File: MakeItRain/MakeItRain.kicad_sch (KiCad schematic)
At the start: 11 parts, among them J1 Conn_02x15_Odd_Even, J2 Conn_02x19_Odd_Even, J3 Conn_01x19

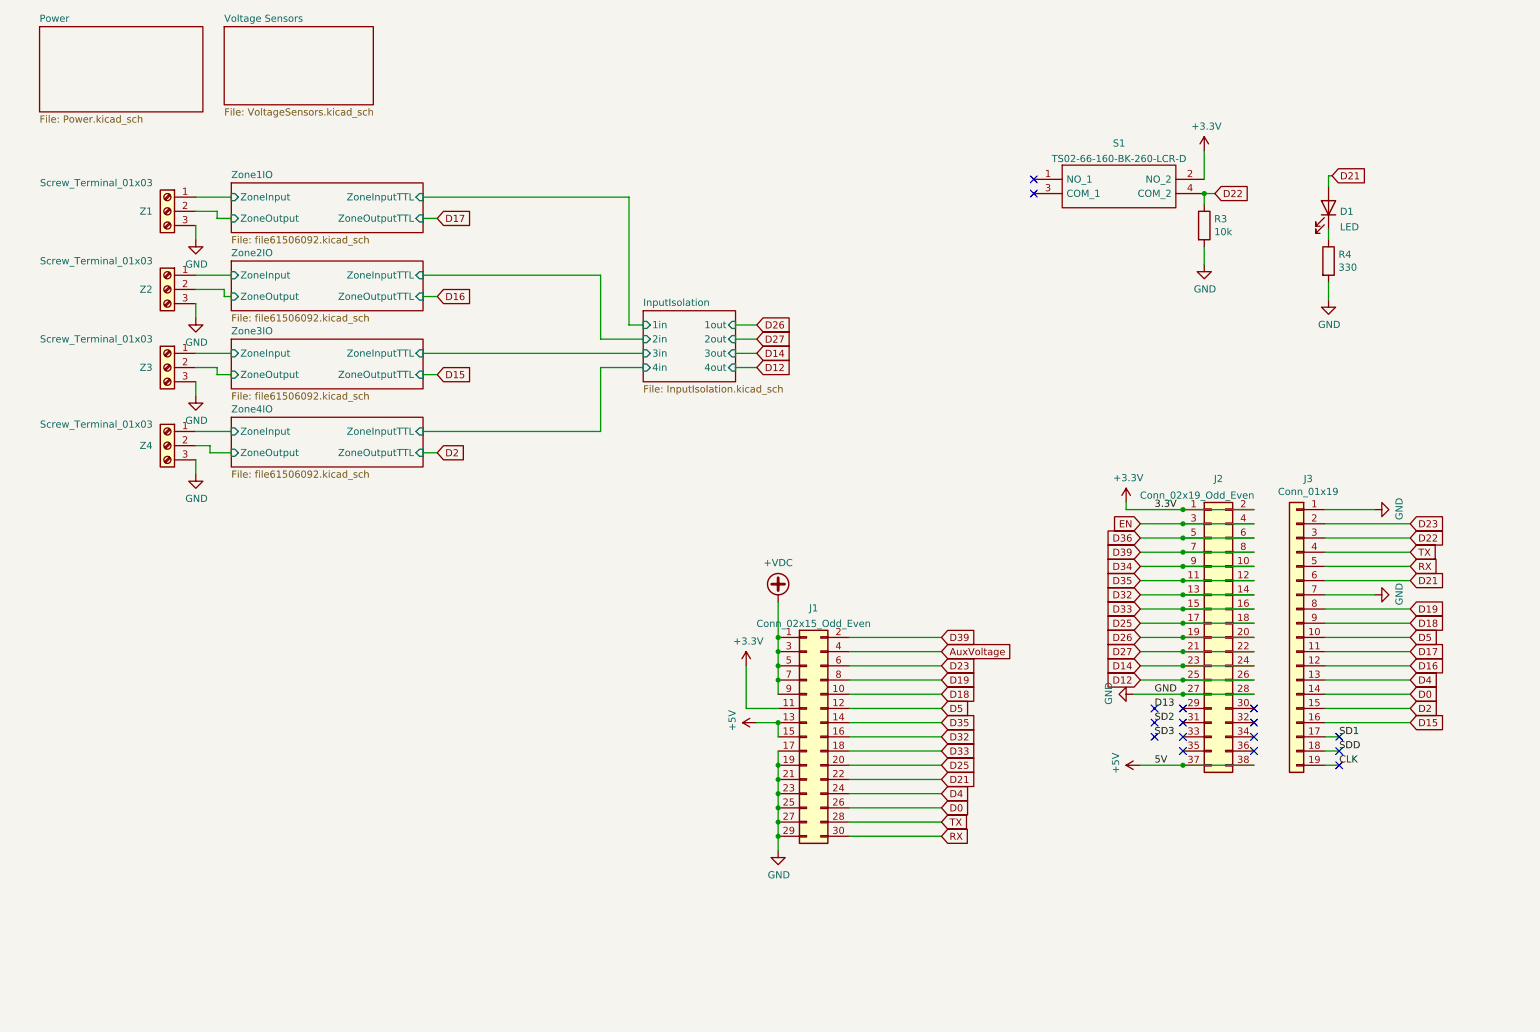
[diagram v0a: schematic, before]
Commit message: working on pin reassignment to fix the stupid stupid ways that esp32 are designed in hardware that require much in way of digging through docs cause not all gpio are created equal.
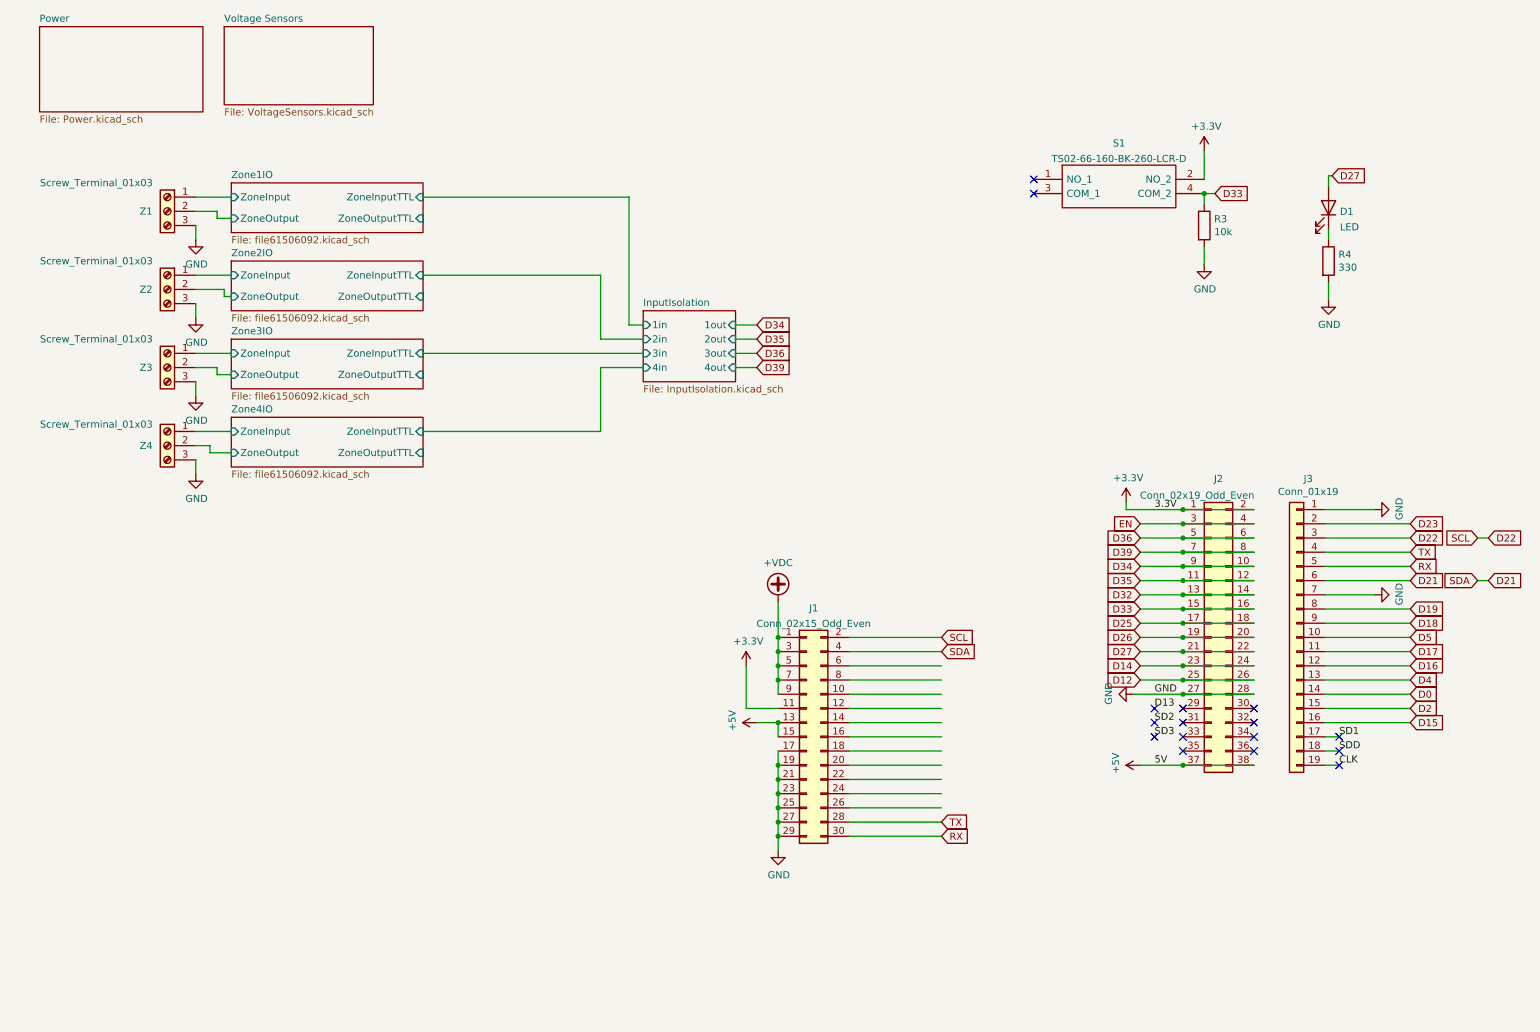
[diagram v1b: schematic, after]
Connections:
- net AuxVoltage is gone; now on net D21: J1.4 (Pin_4)
- net D0: no longer J1.26 (Pin_26)
- net D18: no longer J1.10 (Pin_10)
- net D19: no longer J1.8 (Pin_8)
- net D21: no longer D1.2 (A), J1.22 (Pin_22)
- net D22: now also J1.2 (Pin_2); no longer R3.1, S1.4 (COM_2)
- net D23: no longer J1.6 (Pin_6)
- net D25: no longer J1.20 (Pin_20)
- net D27: now also D1.2 (A)
- net D32: no longer J1.16 (Pin_16)
- net D33: now also R3.1, S1.4 (COM_2); no longer J1.18 (Pin_18)
- net D35: no longer J1.14 (Pin_14)
- net D39: no longer J1.2 (Pin_2)
- net D4: no longer J1.24 (Pin_24)
- net D5: no longer J1.12 (Pin_12)

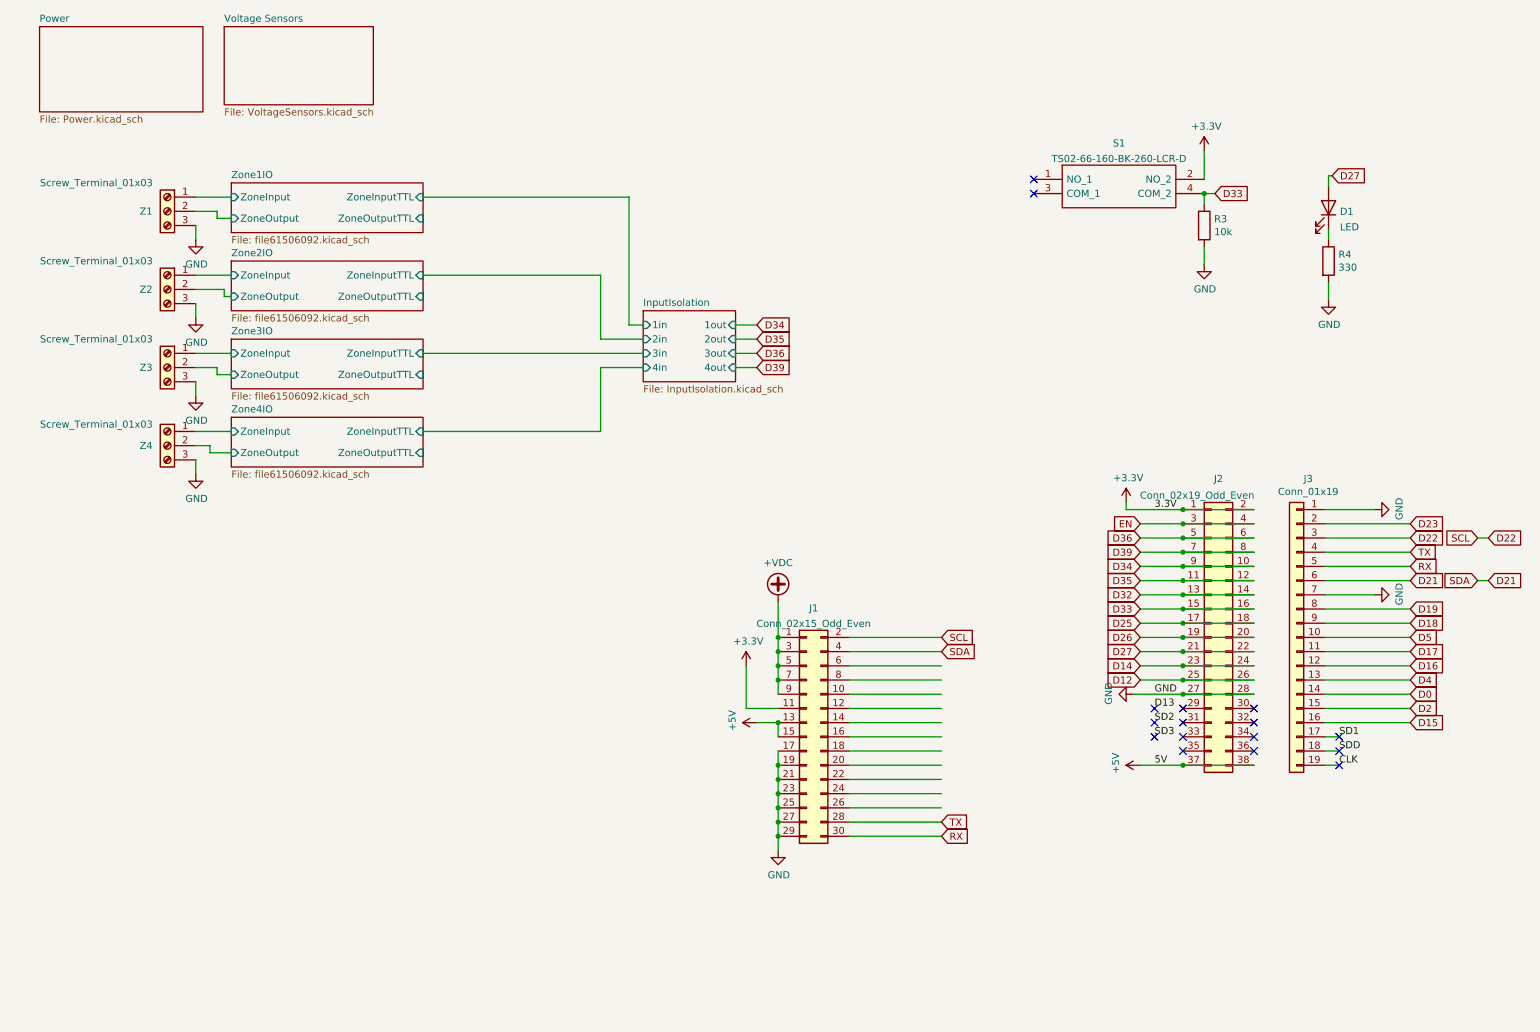
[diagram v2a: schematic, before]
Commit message: starting to add in the mcp23008 to get around the lack of pins or "special" pins that will fuck up designs. stupid ESP32s
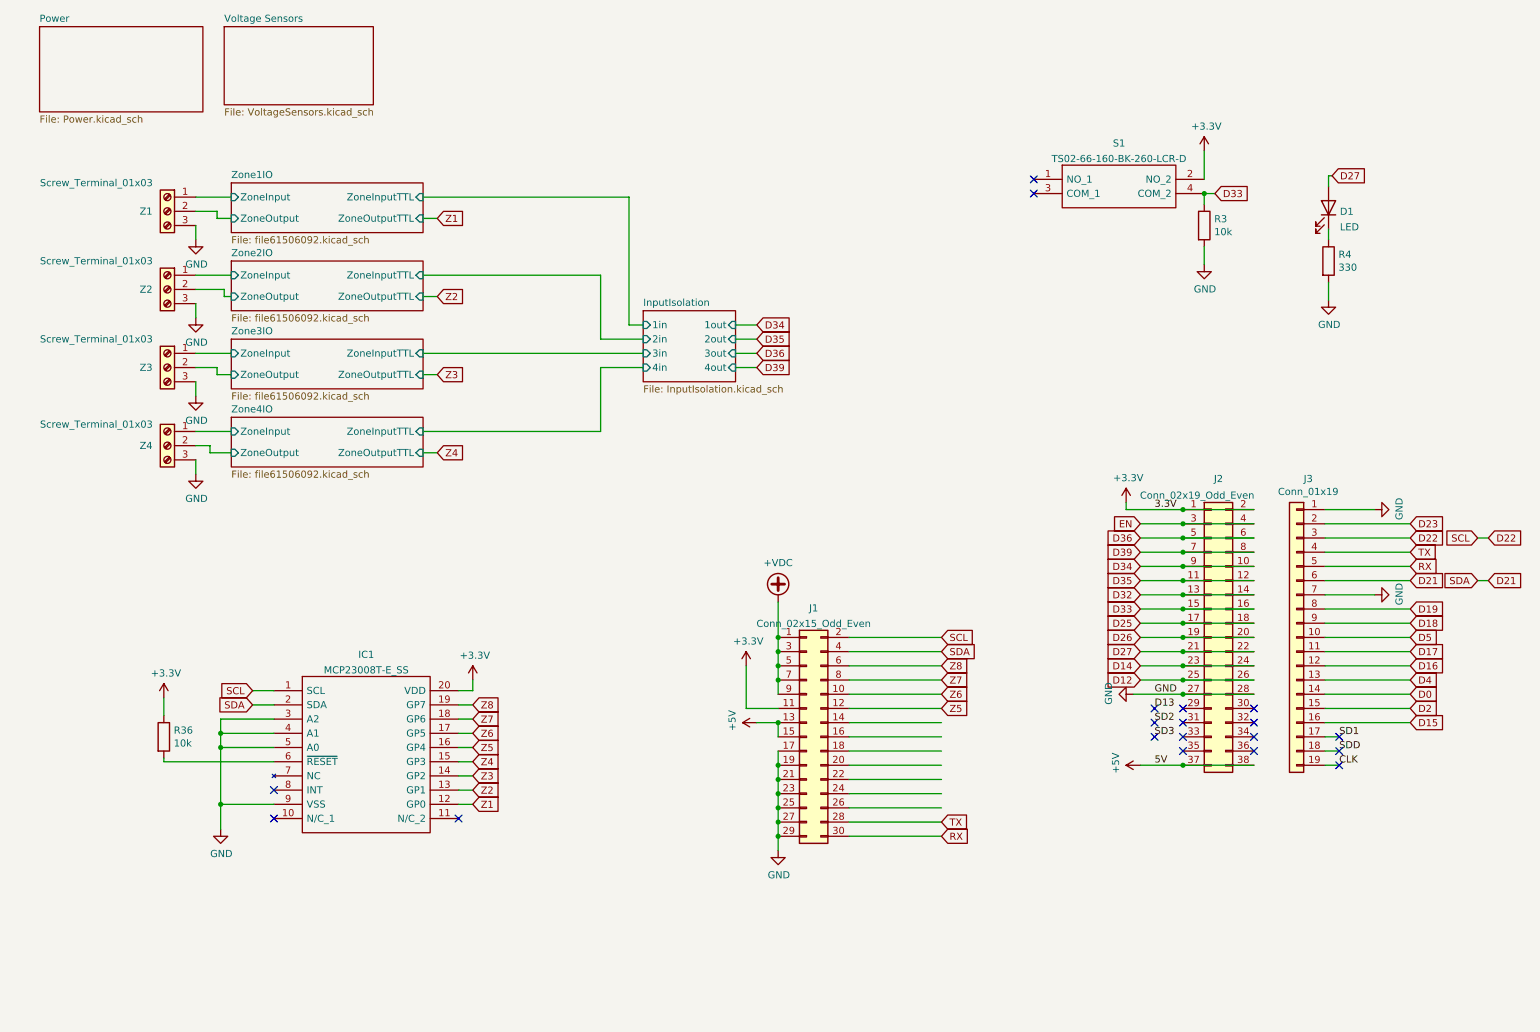
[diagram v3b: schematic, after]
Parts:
- added IC1: MCP23008T-E_SS, SOP65P780X200-20N, symbol Samac_Sys:MCP23008T-E_SS
- added R36: 10k, Resistor_THT:R_Axial_DIN0207_L6.3mm_D2.5mm_P2.54mm_Vertical, symbol Device:R
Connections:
- net +3V3: now also IC1.20 (VDD), R36.1
- net D21: now also IC1.2 (SDA)
- net D22: now also IC1.1 (SCL)
- net GND: now also IC1.3 (A2), IC1.4 (A1), IC1.5 (A0), IC1.9 (VSS)
- net Z6: now reaches J1.10 (Pin_10)
- net Z6: now also IC1.17 (GP5)
- net Z5: now reaches J1.12 (Pin_12)
- net Z5: now also IC1.16 (GP4)
- net Z8: now reaches J1.6 (Pin_6)
- net Z8: now also IC1.19 (GP7)
- net Z7: now reaches J1.8 (Pin_8)
- net Z7: now also IC1.18 (GP6)
- new net: IC1.6 (~{RESET}), R36.2
- new net Z1: IC1.12 (GP0)
- new net Z2: IC1.13 (GP1)
- new net Z3: IC1.14 (GP2)
- new net Z4: IC1.15 (GP3)
- no-connect marks 16 -> 19

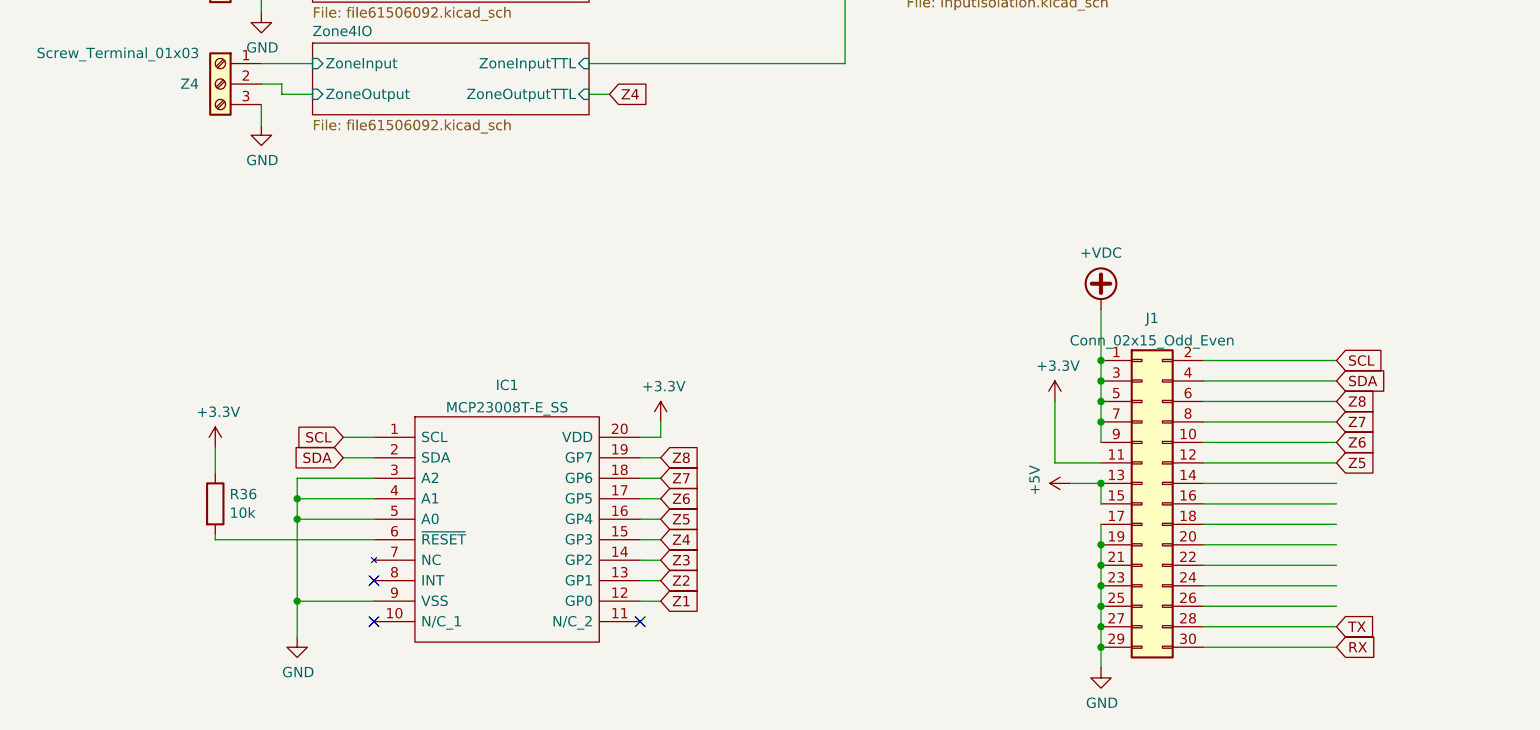
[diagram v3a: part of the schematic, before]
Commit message: i think i have the pins finally figured out. Need to breadboard this setup to make sure it works.
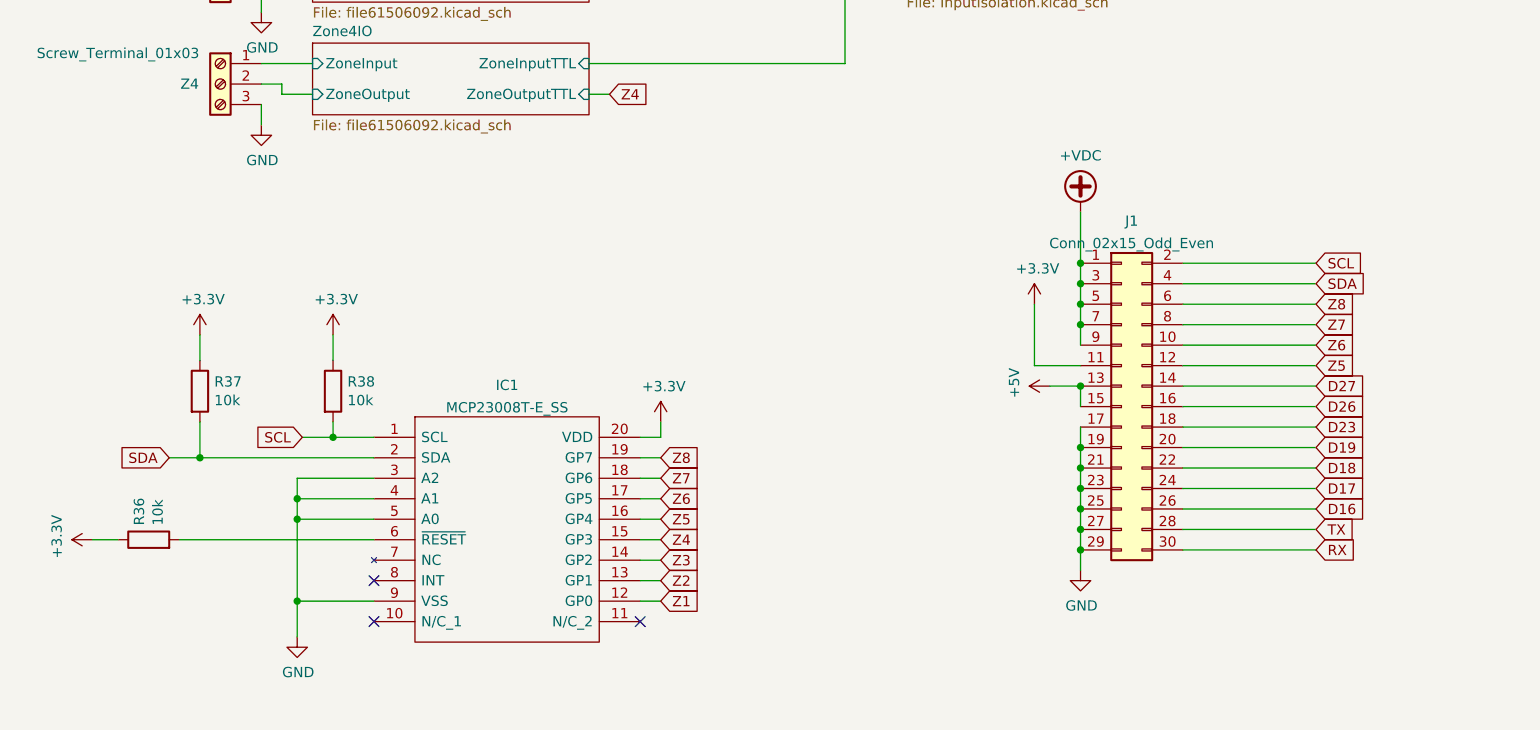
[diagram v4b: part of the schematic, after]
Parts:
- added R37, R38: 10k, Resistor_THT:R_Axial_DIN0207_L6.3mm_D2.5mm_P2.54mm_Vertical, symbol Device:R
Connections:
- net +3V3: now also R37.1, R38.1
- net D16: now also J1.26 (Pin_26)
- net D17: now also J1.24 (Pin_24)
- net D18: now also J1.22 (Pin_22)
- net D19: now also J1.20 (Pin_20)
- net D21: now also R37.2
- net D22: now also R38.2
- net D23: now also J1.18 (Pin_18)
- net D26: now also J1.16 (Pin_16)
- net D27: now also J1.14 (Pin_14)
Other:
- moved on the sheet: J1, R36
